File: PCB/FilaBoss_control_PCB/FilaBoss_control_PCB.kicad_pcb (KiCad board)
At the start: 2 copper layers, 1 part, among them U1 WEMOS_C3_mini

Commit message: pcb v1 ready
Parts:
- added A1: Pololu_Breakout_A4988, Module:Pololu_Breakout-16_15.2x20.3mm, F.Cu at (96.5, 129.5)
- added C1: C, Capacitor_THT:C_Axial_L5.1mm_D3.1mm_P10.00mm_Horizontal, F.Cu at (76.3, 121.9)
- added C2: C, Capacitor_THT:C_Axial_L5.1mm_D3.1mm_P10.00mm_Horizontal, F.Cu at (76.3, 127.0)
- added C3: C, Capacitor_THT:C_Axial_L5.1mm_D3.1mm_P10.00mm_Horizontal, F.Cu at (114.1, 106.7)
- added D1: D, Diode_THT:D_A-405_P10.16mm_Horizontal, F.Cu at (68.6, 94.0)
- added D2: D, Diode_THT:D_A-405_P10.16mm_Horizontal, F.Cu at (53.3, 99.1)
- added F1: Fuse, Fuse:Fuseholder_Clip-5x20mm_Keystone_3512P_Inline_P23.62x7.27mm_D1.02x2.41x1.02x1.57mm_Horizontal, F.Cu at (43.2, 112.1)
- added J1: Conn_01x04_Encoder, PCM_SparkFun-Connector:JST_1x04_P2.0mm_Vertical_PTH, F.Cu at (88.9, 133.3)
- added J2: Screw_Terminal_01x02, TerminalBlock:TerminalBlock_Xinya_XY308-2.54-2P_1x02_P2.54mm_Horizontal, F.Cu at (63.5, 94.0)
- added J3: Screw_Terminal_01x02, TerminalBlock:TerminalBlock_Xinya_XY308-2.54-2P_1x02_P2.54mm_Horizontal, F.Cu at (55.9, 94.0)
- added J5: Barrel_Jack_PTH_Slot, PCM_SparkFun-Connector:Barrel_Jack_PTH_Slot, F.Cu at (45.7, 96.5)
- added J6: PinHeader_01x06_P2.54mm_Vertical_THT_D1mm, PCM_fab:PinHeader_01x06_P2.54mm_Vertical_THT_D1mm, F.Cu at (86.4, 91.4)
- added J7: Conn_01x04, PCM_SparkFun-Connector:JST_1x04_P2.0mm_Vertical_PTH, F.Cu at (104.6, 135.3)
- added J8: JST_2mm_3, PCM_SparkFun-Connector:JST_1x03_P2.0mm_Vertical_PTH, F.Cu at (94.5, 92.0)
- added J9: Conn_01x04_Encoder, PCM_SparkFun-Connector:JST_1x04_P2.0mm_Vertical_PTH, F.Cu at (108.4, 92.0)
- added L1: L, Inductor_THT_Wurth:L_Wurth_WE-HCFT-2012_LeadDiameter1.2mm, F.Cu at (50.7, 127.0)
- added Q1: IRLZ44N, Package_TO_SOT_THT:TO-220-3_Vertical, F.Cu at (58.4, 106.7)
- added Q2: IRLZ44N, Package_TO_SOT_THT:TO-220-3_Vertical, F.Cu at (63.5, 106.7)
- added R1: 100R, Resistor_THT:R_Axial_DIN0207_L6.3mm_D2.5mm_P10.16mm_Horizontal, F.Cu at (78.7, 96.5)
- added R2: 10K, Resistor_THT:R_Axial_DIN0207_L6.3mm_D2.5mm_P10.16mm_Horizontal, F.Cu at (73.7, 101.7)
- added R3: 10K, Resistor_THT:R_Axial_DIN0207_L6.3mm_D2.5mm_P10.16mm_Horizontal, F.Cu at (73.7, 106.7)
- added R4: 100R, Resistor_THT:R_Axial_DIN0207_L6.3mm_D2.5mm_P10.16mm_Horizontal, F.Cu at (78.7, 111.8)
- added U2: LM78M05_TO220, Package_TO_SOT_THT:TO-220-3_Vertical, F.Cu at (71.1, 127.0)
- U1: value WEMOS_C3_mini -> ESP32_C3_super_mini; footprint RF_Module:WEMOS_C3_mini -> custom:ESP32-super-mini
- moved U1 31.8 mm to (106.7, 104.1), turned to -90 degrees
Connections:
- U1 pad 1: unconnected-(U1-EN-Pad1) -> Net-(A1-STEP)
- U1 pad 10: unconnected-(U1-GND-Pad10) -> Net-(J9-Pin_3)
- U1 pad 11: unconnected-(U1-D6-Pad11) -> +3.3V
- U1 pad 12: unconnected-(U1-D7-Pad12) -> GND
- U1 pad 13: unconnected-(U1-D8-Pad13) -> +5V
- U1 pad 2: unconnected-(U1-D3-Pad2) -> Net-(J1-Pin_2)
- U1 pad 3: unconnected-(U1-D2-Pad3) -> Net-(J1-Pin_1)
- U1 pad 4: unconnected-(U1-D1-Pad4) -> Net-(U1-D2/A2)
- U1 pad 5: unconnected-(U1-D0-Pad5) -> Net-(U1-D3/A3)
- U1 pad 6: unconnected-(U1-D4-Pad6) -> Net-(J6-Pin_4)
- U1 pad 7: unconnected-(U1-D5-Pad7) -> Net-(J6-Pin_3)
- U1 pad 8: unconnected-(U1-3V3-Pad8) -> Net-(J9-Pin_1)
- U1 pad 9: unconnected-(U1-VBus-Pad9) -> Net-(J9-Pin_2)
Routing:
- net GND: track 0.00 -> 106.7 mm, vias 0 -> 4
- net Net-(J6-Pin_4): track 0.00 -> 43.3 mm
- net Net-(J6-Pin_3): track 0.00 -> 39.8 mm
- net Net-(J1-Pin_1): track 0.00 -> 39.2 mm
- net Net-(J1-Pin_2): track 0.00 -> 34.5 mm
- net Net-(Q1-G): track 0.00 -> 27.4 mm
- net Net-(U1-D3/A3): track 0.00 -> 26.9 mm
- net Net-(U1-D2/A2): track 0.00 -> 20.5 mm
- net Net-(Q2-G): track 0.00 -> 19.6 mm
- net Net-(D2-A): track 0.00 -> 19.1 mm
- net Net-(D1-K): track 0.00 -> 18.6 mm
- net Net-(D1-A): track 0.00 -> 16.7 mm
- net Net-(J9-Pin_3): track 0.00 -> 7.91 mm
- net Net-(J9-Pin_2): track 0.00 -> 7.56 mm
- net Net-(J9-Pin_1): track 0.00 -> 7.04 mm
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- added copper zone on F.Cu, net +24V
- added copper zone on F.Cu, net +3.3V
- added copper zone on F.Cu, net +5V
- added copper zone on B.Cu, net GND
- added copper zone on F.Cu, net LINE
- added copper zone on F.Cu, net VDC
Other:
- board outline added: 81.3 x 53.3 mm

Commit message: forgot custom lib
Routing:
- net Net-(J6-Pin_4): track 43.3 -> 44.4 mm
- net Net-(J6-Pin_3): track 39.8 -> 40.5 mm
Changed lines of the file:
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@@
 		(allow_soldermask_bridges_in_footprints no)
 		(tenting front back)
+		(grid_origin 38.1 86.36)
 		(pcbplotparams
-			(layerselection 0x00000000_00000000_55555555_5755f5ff)
+			(layerselection 0x00000000_00000000_55555555_57555555)
 			(plot_on_all_layers_selection 0x00000000_00000000_00000000_00000000)
 			(disableapertmacros no)
@@
 			(usegerberattributes yes)
 			(usegerberadvancedattributes yes)
-			(creategerberjobfile yes)
+			(creategerberjobfile no)
 			(dashed_line_dash_ratio 12.000000)
 			(dashed_line_gap_ratio 3.000000)
@@
 			(plotframeref no)
 			(mode 1)
-			(useauxorigin no)
+			(useauxorigin yes)
 			(hpglpennumber 1)
 			(hpglpenspeed 20)
@@
 			(outputformat 1)
 			(mirror no)
-			(drillshape 1)
+			(drillshape 0)
 			(scaleselection 1)
 			(outputdirectory "")
@@
 			(pinfunction "3V3")
 			(pintype "output")
+			(thermal_bridge_width 1)
 		)
 		(pad "12" thru_hole circle
@@
 			(pinfunction "5V")
 			(pintype "power_in")
+			(thermal_bridge_width 1)
 		)
 		(pad "20" thru_hole circle
@@
 			(pinfunction "S")
 			(pintype "passive")
+			(thermal_bridge_angle 45)
 		)
 		(embedded_fonts no)
@@
 			(pinfunction "Pin_2")
 			(pintype "passive")
+			(thermal_bridge_angle 45)
 		)
 		(pad "3" thru_hole oval
@@
 			(pinfunction "K")
 			(pintype "passive")
+			(thermal_bridge_angle 45)
 		)
 		(pad "2" thru_hole circle
@@
 			(pinfunction "VI")
 			(pintype "power_in")
+			(thermal_bridge_angle 45)
 		)
 		(pad "2" thru_hole oval
@@
 			(pinfunction "GND")
 			(pintype "power_in")
+			(thermal_bridge_angle 45)
 		)
 		(pad "3" thru_hole oval
@@
 			(pinfunction "VO")
 			(pintype "power_out")
+			(thermal_bridge_angle 45)
 		)
 		(embedded_fonts no)
@@
 			(pinfunction "Pin_3")
 			(pintype "passive")
+			(thermal_bridge_width 1)
 		)
 		(pad "4" thru_hole circle
@@
 			(pinfunction "S")
 			(pintype "passive")
+			(thermal_bridge_angle 45)
 		)
 		(embedded_fonts no)
@@
 			(pinfunction "GND")
 			(pintype "power_in")
+			(thermal_bridge_angle 45)
 		)
 		(pad "2" thru_hole oval
@@
 			(pinfunction "VDD")
 			(pintype "power_in")
+			(thermal_bridge_width 1)
 			(thermal_bridge_angle 45)
 		)
@@
 			(pinfunction "GND")
 			(pintype "power_in")
+			(thermal_bridge_angle 45)
 		)
 		(pad "8" thru_hole oval
@@
 			(pinfunction "VMOT")
 			(pintype "power_in")
+			(thermal_bridge_angle 45)
 		)
 		(pad "9" thru_hole oval
@@
 			(pinfunction "~{ENABLE}")
 			(pintype "input")
+			(thermal_bridge_angle 45)
 		)
 		(pad "10" thru_hole oval
@@
 			(pinfunction "MS1")
 			(pintype "input")
+			(thermal_bridge_angle 45)
 		)
 		(pad "11" thru_hole oval
@@
 			(pinfunction "MS2")
 			(pintype "input")
+			(thermal_bridge_angle 45)
 		)
 		(pad "12" thru_hole oval
@@
 			(pinfunction "MS3")
 			(pintype "input")
+			(thermal_bridge_angle 45)
 		)
 		(pad "13" thru_hole oval
@@
 			(pinfunction "~{RESET}")
 			(pintype "input")
+			(thermal_bridge_angle 45)
 		)
 		(pad "14" thru_hole oval
@@
 			(pinfunction "~{SLEEP}")
 			(pintype "input")
+			(thermal_bridge_angle 45)
 		)
 		(pad "15" thru_hole oval
@@
 			(pinfunction "1")
 			(pintype "passive")
-			(thermal_bridge_angle 0)
 		)
 		(pad "2" thru_hole circle
@@
 	)
 	(segment
-		(start 109.22 96.52)
-		(end 112.811 92.929)
+		(start 83.82 88.9)
+		(end 81.28 91.44)
 		(width 0.4)
 		(layer "F.Cu")
@@
 	)
 	(segment
-		(start 112.811 92.929)
-		(end 112.811 90.859686)
+		(start 112.811 90.859686)
+		(end 110.851314 88.9)
 		(width 0.4)
 		(layer "F.Cu")
@@
 	)
 	(segment
-		(start 111.715385 89.764071)
-		(end 82.955929 89.764071)
+		(start 110.851314 88.9)
+		(end 83.82 88.9)
 		(width 0.4)
 		(layer "F.Cu")
@@
 	)
 	(segment
-		(start 82.955929 89.764071)
-		(end 81.28 91.44)
+		(start 112.811 92.929)
+		(end 112.811 90.859686)
 		(width 0.4)
 		(layer "F.Cu")
@@
 	)
 	(segment
-		(start 112.811 90.859686)
-		(end 111.715385 89.764071)
+		(start 109.22 96.52)
+		(end 112.811 92.929)
 		(width 0.4)
 		(layer "F.Cu")
@@
 	)
 	(segment
-		(start 113.612 90.527901)
-		(end 113.612 94.668)
+		(start 82.55 87.63)
+		(end 110.714099 87.63)
 		(width 0.4)
 		(layer "F.Cu")
@@
 	)
 	(segment
-		(start 113.612 94.668)
-		(end 111.76 96.52)
+		(start 78.74 91.44)
+		(end 82.55 87.63)
 		(width 0.4)
 		(layer "F.Cu")
@@
 	)
 	(segment
-		(start 112.047171 88.963071)
-		(end 113.612 90.527901)
+		(start 113.612 94.668)
+		(end 111.76 96.52)
 		(width 0.4)
 		(layer "F.Cu")
@@
 	)
 	(segment
-		(start 81.216929 88.963071)
-		(end 112.047171 88.963071)
+		(start 113.612 90.527901)
+		(end 113.612 94.668)
 		(width 0.4)
 		(layer "F.Cu")
@@
 	)
 	(segment
-		(start 78.74 91.44)
-		(end 81.216929 88.963071)
+		(start 110.714099 87.63)
+		(end 113.612 90.527901)
 		(width 0.4)
 		(layer "F.Cu")
@@
 	)
 	(segment
-		(start 93.648214 108.419)
-		(end 92.847214 109.22)
+		(start 101.931785 108.419)
+		(end 93.648214 108.419)
 		(width 0.4)
 		(layer "F.Cu")
@@
 	)
 	(segment
-		(start 101.931785 108.419)
-		(end 93.648214 108.419)
+		(start 104.14 109.22)
+		(end 102.732786 109.22)
 		(width 0.4)
 		(layer "F.Cu")
@@
 	)
 	(segment
-		(start 106.68 111.76)
-		(end 104.14 109.22)
+		(start 91.44 109.22)
+		(end 88.9 111.76)
 		(width 0.4)
 		(layer "F.Cu")
@@
 	)
 	(segment
-		(start 92.847214 109.22)
-		(end 91.44 109.22)
+		(start 102.732786 109.22)
+		(end 101.931785 108.419)
 		(width 0.4)
 		(layer "F.Cu")
@@
 	)
 	(segment
-		(start 91.44 109.22)
-		(end 88.9 111.76)
+		(start 93.648214 108.419)
+		(end 92.847214 109.22)
 		(width 0.4)
 		(layer "F.Cu")
@@
 	)
 	(segment
-		(start 104.14 109.22)
-		(end 102.732786 109.22)
+		(start 106.68 111.76)
+		(end 104.14 109.22)
 		(width 0.4)
 		(layer "F.Cu")
@@
 	)
 	(segment
-		(start 102.732786 109.22)
-		(end 101.931785 108.419)
+		(start 92.847214 109.22)
+		(end 91.44 109.22)
 		(width 0.4)
 		(layer "F.Cu")

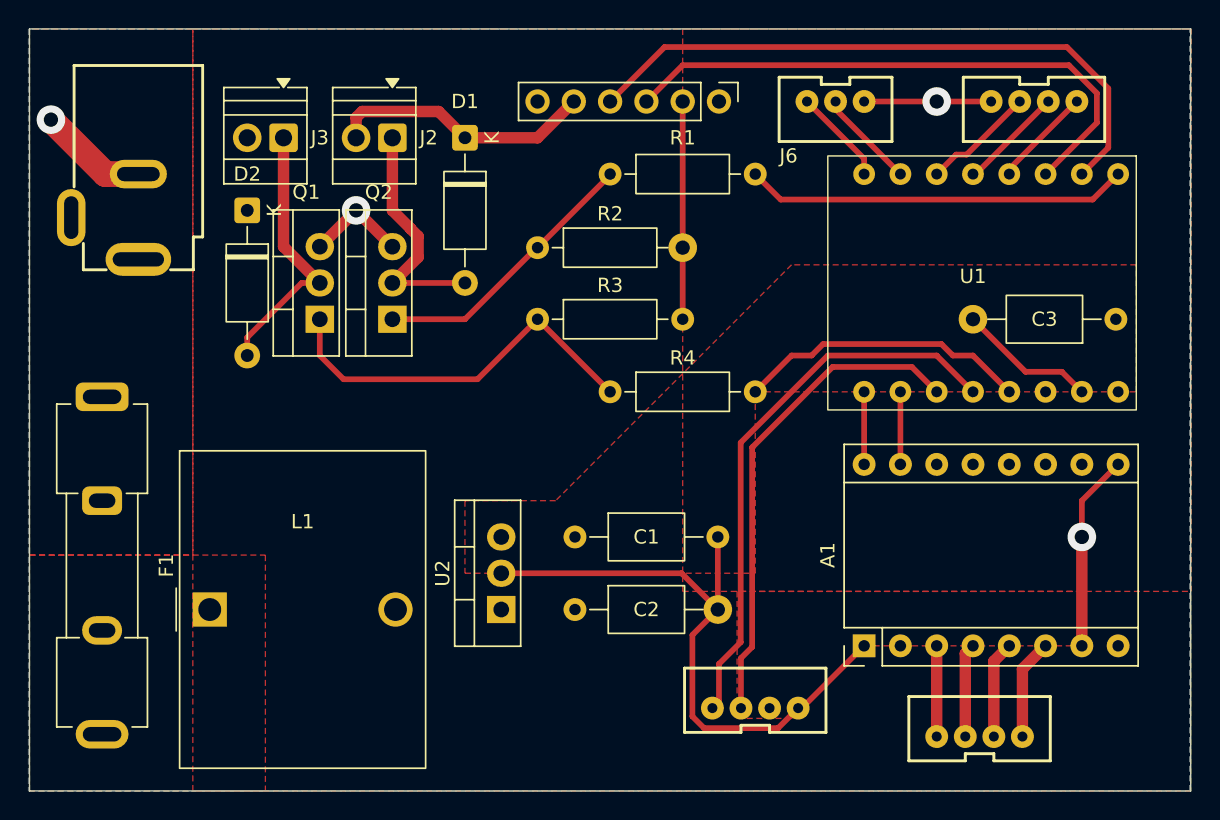
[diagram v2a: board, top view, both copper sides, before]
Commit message: bigger esp required
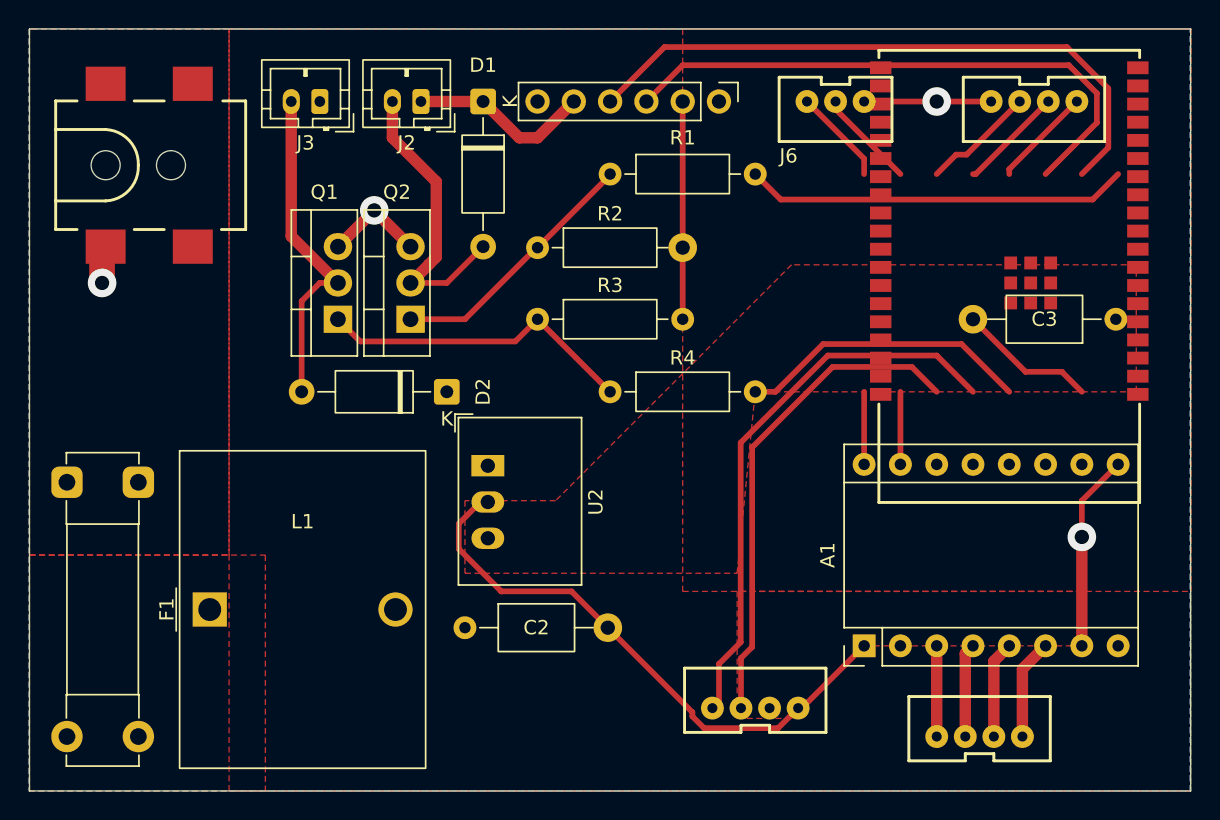
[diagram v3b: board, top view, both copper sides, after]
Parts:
- removed C1: C, Capacitor_THT:C_Axial_L5.1mm_D3.1mm_P10.00mm_Horizontal
- F1: footprint Fuse:Fuseholder_Clip-5x20mm_Keystone_3512P_Inline_P23.62x7.27mm_D1.02x2.41x1.02x1.57mm_Horizontal -> Fuse:Fuseholder_Clip-5x20mm_Bel_FC-203-22_Lateral_P17.80x5.00mm_D1.17mm_Horizontal
- J2, J3: value Screw_Terminal_01x02 -> JST_2mm_LiPo; footprint TerminalBlock:TerminalBlock_Xinya_XY308-2.54-2P_1x02_P2.54mm_Horizontal -> Connector_JST:JST_PH_B2B-PH-K_1x02_P2.00mm_Vertical
- J5: value Barrel_Jack_PTH_Slot -> Barrel_Jack_SMD; footprint PCM_SparkFun-Connector:Barrel_Jack_PTH_Slot -> PCM_SparkFun-Connector:Barrel_Jack_SMD
- U1: value ESP32_C3_super_mini -> ESP32-WROVER-E-N16R8; footprint custom:ESP32-super-mini -> PCM_SparkFun-RF:ESP32-WROVER-E-IE
- U2: value LM78M05_TO220 -> R-78E5.0-0.5; footprint Package_TO_SOT_THT:TO-220-3_Vertical -> Converter_DCDC:Converter_DCDC_RECOM_R-78E-0.5_THT
- moved D2 18.9 mm to (67.3, 111.8), turned to 180 degrees
- moved U2 10.1 mm to (70.2, 116.9), turned to -90 degrees
- moved C2 7.80 mm to (68.6, 128.3)
- moved F1 6.50 mm to (45.7, 118.1)
- moved J3 3.59 mm to (58.4, 91.4)
- moved J2 3.23 mm to (65.5, 91.4)
- moved D1 2.84 mm to (69.8, 91.4)
- moved J5 2.37 mm to (43.4, 95.9), turned to 0 degrees
- moved Q1 1.27 mm to (59.7, 106.7)
- moved Q2 1.27 mm to (64.8, 106.7)
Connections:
- A1 pad 15: Net-(A1-STEP) -> unconnected-(A1-STEP-Pad15)
- A1 pad 16: Net-(A1-DIR) -> GND
- C3 pad 2: GND -> unconnected-(C3-Pad2)
- J1 pad 1: Net-(J1-Pin_1) -> unconnected-(J1-Pin_1-Pad1)
- J1 pad 2: Net-(J1-Pin_2) -> unconnected-(J1-Pin_2-Pad2)
- J2 pad 1: Net-(D1-A) -> Net-(D1-K)
- J2 pad 2: Net-(D1-K) -> Net-(D1-A)
- J3 pad 1: Net-(D2-A) -> +24V
- J3 pad 2: +24V -> Net-(D2-A)
- J6 pad 4: Net-(J6-Pin_4) -> unconnected-(J6-Pin_4-Pad4)
- J8 pad 2: Net-(U1-D7/RX) -> unconnected-(J8-Pad2)
- J8 pad 3: Net-(U1-D6/TX) -> unconnected-(J8-Pad3)
- R1 pad 2: Net-(U1-D3/A3) -> unconnected-(R1-Pad2)
- R4 pad 2: Net-(U1-D2/A2) -> unconnected-(R4-Pad2)
- U1 pad 1: Net-(A1-STEP) -> Net-(U1-GND-Pad1)
- U1 pad 10: Net-(J9-Pin_3) -> unconnected-(U1-IOA25-Pad10)
- U1 pad 11: +3.3V -> unconnected-(U1-IOA26-Pad11)
- U1 pad 12: GND -> unconnected-(U1-IOA27-Pad12)
- U1 pad 13: +5V -> unconnected-(U1-IOA14-Pad13)
- U1 pad 2: Net-(J1-Pin_2) -> Net-(J6-Pin_3)
- U1 pad 20: Net-(U1-D7/RX) -> unconnected-(U1-NC-Pad20)
- U1 pad 21: Net-(U1-D6/TX) -> unconnected-(U1-NC-Pad21)
- U1 pad 3: Net-(J1-Pin_1) -> unconnected-(U1-EN-Pad3)
- U1 pad 4: Net-(U1-D2/A2) -> unconnected-(U1-IA36-Pad4)
- U1 pad 5: Net-(U1-D3/A3) -> unconnected-(U1-IA39-Pad5)
- U1 pad 6: Net-(J6-Pin_4) -> unconnected-(U1-IA34-Pad6)
- U1 pad 7: Net-(J6-Pin_3) -> unconnected-(U1-IA35-Pad7)
- U1 pad 8: Net-(J9-Pin_1) -> unconnected-(U1-IOA32-Pad8)
- U1 pad 9: Net-(J9-Pin_2) -> unconnected-(U1-IOA33-Pad9)
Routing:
- net (no net): track 0.00 -> 93.6 mm
- net unconnected-(J6-Pin_4-Pad4): track 0.00 -> 44.4 mm
- net Net-(J6-Pin_4): track 44.4 -> 0.00 mm
- net Net-(J1-Pin_1): track 39.2 -> 0.00 mm
- net Net-(J1-Pin_2): track 34.5 -> 0.00 mm
- net Net-(J6-Pin_3): track 40.5 -> 75.1 mm
- net Net-(U1-D3/A3): track 26.9 -> 0.00 mm
- net Net-(U1-D2/A2): track 20.5 -> 0.00 mm
- net GND: track 106.7 -> 93.3 mm
- net unconnected-(C3-Pad2): track 0.00 -> 9.72 mm
- net Net-(U1-D7/RX): track 6.96 -> 0.00 mm
- net unconnected-(J8-Pad3): track 0.00 -> 6.74 mm
- net Net-(U1-D6/TX): track 6.74 -> 0.00 mm
- net Net-(D1-K): track 18.6 -> 12.8 mm
- net unconnected-(A1-STEP-Pad15): track 0.00 -> 5.08 mm
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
